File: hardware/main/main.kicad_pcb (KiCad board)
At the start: 4 copper layers, 59.7 x 109.5 mm, 220 parts, among them J101 ST_LINK, J102 USART, J301 Overvoltage_protection, J302 Rad_sensor, J303 Mos_temp, J304 Diode_temp, J601 Supplies, J801 RJ45_Shielded, J802 RJ45_Shielded, Q401 BSC093N15NS5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

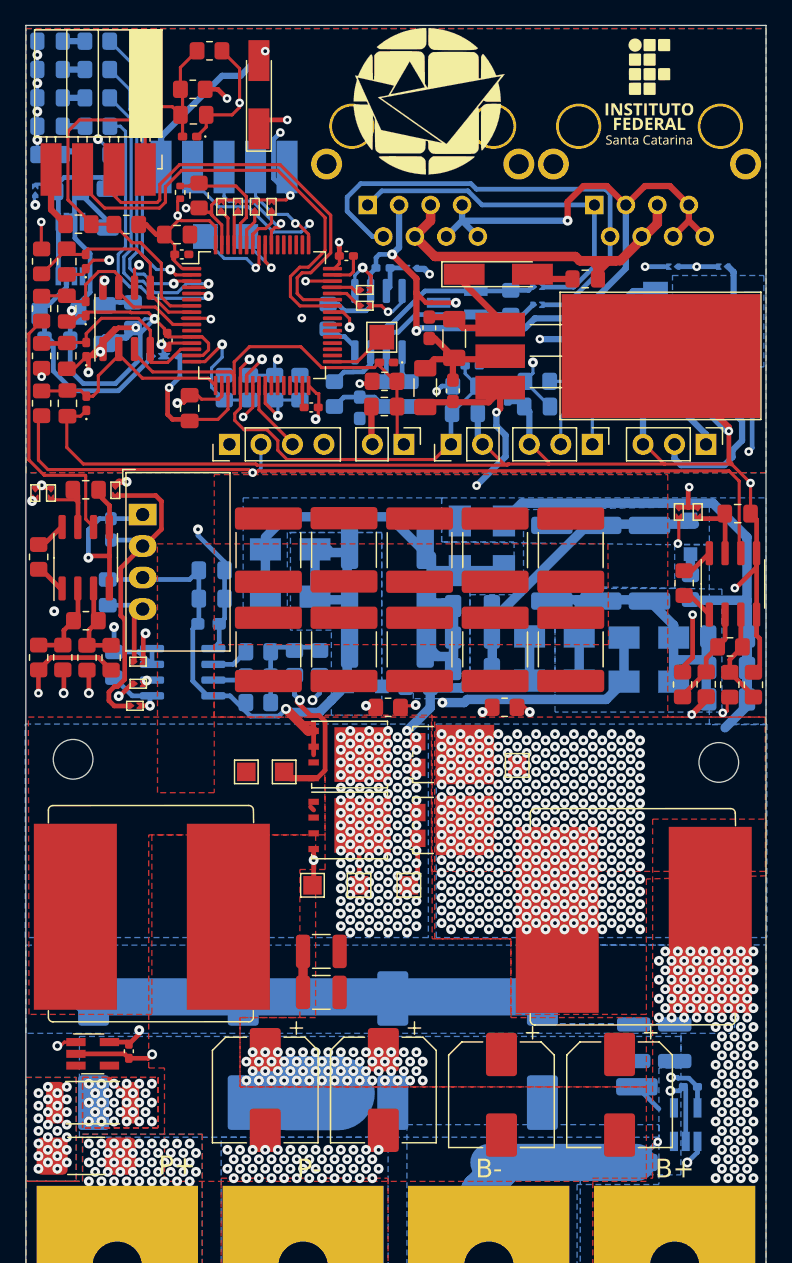
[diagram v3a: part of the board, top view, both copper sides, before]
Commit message: Layout: Silkscreen updated
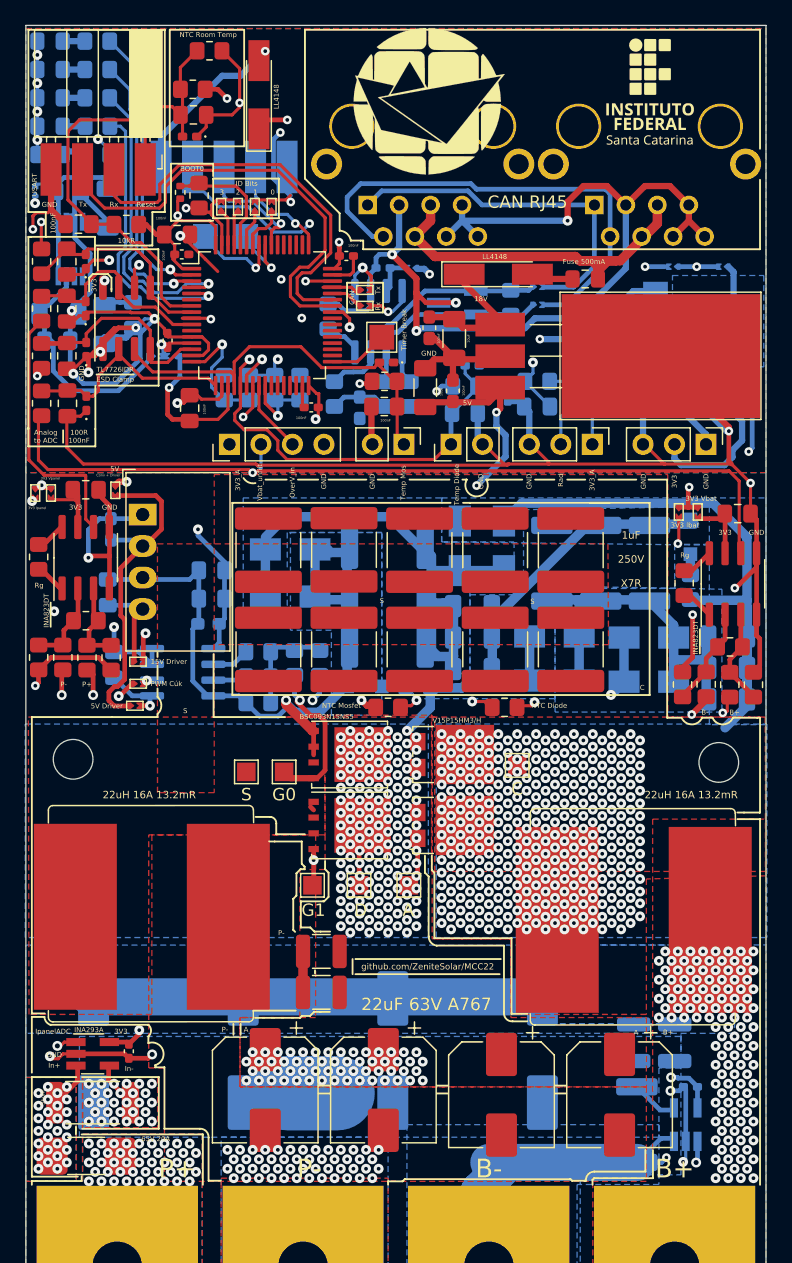
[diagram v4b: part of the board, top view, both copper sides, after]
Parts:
- added LOGO103: Logo_Open_Hardware_Small, Symbol:OSHW-Logo_5.7x6mm_SilkScreen, B.Cu at (30.8, 117.0)
- added LOGO104: Logo_Open_Hardware_Small, Zenite:symbol_logoZenite_small, B.Cu at (23.1, 117.3)
- added LOGO105: Logo_Open_Hardware_Small, Zenite:synbol_logoifsc_small, B.Cu at (37.7, 104.9)
- moved LOGO102 0.05 mm to (69.1, 87.9)
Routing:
- net GND: track 608.7 -> 973.5 mm, vias 32 -> 38
- net (no net): track 0.00 -> 4.76 mm
- net /B-: track 62.2 -> 66.8 mm
- net Net-(R321-Pad1): track 130.5 -> 133.9 mm
- net /P+: track 36.2 -> 39.0 mm
- net /Cuk/S: track 91.6 -> 90.3 mm
- net Net-(R320-Pad1): track 58.8 -> 59.7 mm
- net /Cuk/A: track 54.2 -> 54.9 mm
- net /P-: track 53.3 -> 53.9 mm
- net /Cuk/C: vias 352 -> 351
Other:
- board text added: "0"
- board text added: "1"
- board text added: "100R 100nF"
- board text added: "100V 10uF"
- board text added: "100nF"
- board text added: "10k"
- board text added: "10kR"
- board text added: "10nF"
- board text added: "10uF"
- board text added: "15V"
- board text added: "15V Driver"
- board text added: "18V"
- board text added: "1EDI60N12AF"
- board text added: "1R"
- board text added: "1uF"
- board text added: "1uF 250V X7R"
- board text added: "2"
- board text added: "22uF 100V"
- board text added: "22uF 63V A767"
- board text added: "22uH 16A 13.2mR"
- board text added: "3"
- board text added: "300R"
- board text added: "3V Ref"
- board text added: "3V3"
- board text added: "3V3 ADC"
- board text added: "3V3 Analog"
- board text added: "3V3 Ibat"
- board text added: "3V3 Ipanel"
- board text added: "3V3 MCU"
- board text added: "3V3 MCU|or| 3V Ref"
- board text added: "3V3 STM"
- board text added: "3V3 Vbat"
- board text added: "3V3 Vpanel"
- board text added: "3V3_A"
- board text added: "4.7nF"
- board text added: "4.7uF"
- board text added: "4R7"
- board text added: "4k7"
- board text added: "520R"
- board text added: "5V"
- board text added: "5V > 3V3"
- board text added: "5V CAN"
- board text added: "5V Driver"
- board text added: "5V STM"
- board text added: "65V 20A"
- board text added: "A"
- board text added: "A767"
- board text added: "AMS1117-3.3"
- board text added: "Analog to ADC"
- board text added: "BOOT0"
- board text added: "BSC093N15NS5"
- board text added: "Bat OverV"
- board text added: "C"
- board text added: "CAN"
- board text added: "CAN Busy"
- board text added: "CAN RJ45"
- board text added: "CAN_H"
- board text added: "CAN_H> <CAN_L"
- board text added: "CAN_L"
- board text added: "CAN_Rx>"
- board text added: "CAN_Tx <"
- board text added: "Conv + Driver"
- board text added: "D"
- board text added: "DB_0"
- board text added: "DB_1"
- board text added: "Diode°C"
- board text added: "Driver"
- board text added: "ESD Clamp"
- board text added: "Fuse 500mA"
- board text added: "G0"
- board text added: "G1"
- board text added: "GND"
- board text added: "ID Bits"
- board text added: "INA293A"
- board text added: "INA823DT"
- board text added: "IbatADC"
- board text added: "In+"
- board text added: "In-"
- board text added: "IpanelADC"
- board text added: "LED0"
- board text added: "LED1"
- board text added: "LL4148"
- board text added: "MCP2551"
- board text added: "Mos.°C"
- board text added: "NTC Diode"
- board text added: "NTC Mosfet"
- board text added: "NTC Room Temp"
- board text added: "Out_G"
- board text added: "OverV_in"
- board text added: "Overvoltage"
- board text added: "P+ Fused"
- board text added: "P+ Unfused"
- board text added: "PESD1CAN"
- board text added: "PWM"
- board text added: "PWM Cúk"
- board text added: "REF3430QDGKRQ1"
- board text added: "Rad"
- board text added: "Rad Sensor"
- board text added: "Reset"
- board text added: "Rg"
- board text added: "Rx"
- board text added: "S"
- board text added: "SNK"
- board text added: "SRC"
- board text added: "ST-Link"
- board text added: "SWCLK"
- board text added: "SWDIO"
- board text added: "SWO"
- board text added: "Shunt"
- board text added: "Snubber"
- board text added: "Status LED"
- board text added: "Supplies"
- board text added: "Supply ADC"
- board text added: "TL7726IDR"
- board text added: "Temp Diode"
- board text added: "Temp Mos"
- board text added: "Timer Break"
- board text added: "Tx"
- board text added: "USART"
- board text added: "V15P15HM3/H"
- board text added: "Vbat_unfilt"
- board text added: "X7R"
- board text added: "github.com/ZeniteSolar/MCC22"

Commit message: layout: Separating analogical power nets
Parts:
- removed D303, D304, D305, D306, D307, D308: ESD351DPYR, Diode_SMD:D_0402_1005Metric_Pad0.77x0.64mm_HandSolder
- added D103: ESD351DPYR, Diode_SMD:D_0402_1005Metric_Pad0.77x0.64mm_HandSolder, B.Cu at (33.8, 97.0)
- added D104: ESD351DPYR, Diode_SMD:D_0402_1005Metric_Pad0.77x0.64mm_HandSolder, B.Cu at (36.1, 97.0)
- added D105: ESD351DPYR, Diode_SMD:D_0402_1005Metric_Pad0.77x0.64mm_HandSolder, B.Cu at (38.4, 97.0)
- added D106: ESD351DPYR, Diode_SMD:D_0402_1005Metric_Pad0.77x0.64mm_HandSolder, F.Cu at (31.5, 92.2)
- added D107: ESD351DPYR, Diode_SMD:D_0402_1005Metric_Pad0.77x0.64mm_HandSolder, F.Cu at (42.9, 96.8)
- added D108: ESD351DPYR, Diode_SMD:D_0402_1005Metric_Pad0.77x0.64mm_HandSolder, F.Cu at (41.4, 96.8)
- added D413: SMF64A, Diode_SMD:D_SOD-123F, B.Cu at (73.9, 164.6)
- added D601: ESD351DPYR, Diode_SMD:D_0402_1005Metric_Pad0.77x0.64mm_HandSolder, B.Cu at (67.8, 107.4)
- added NT101: NetTie_2, Resistor_SMD:R_0201_0603Metric, F.Cu at (11.9, 100.1)
- added NT102: NetTie_2, Resistor_SMD:R_0201_0603Metric, F.Cu at (14.4, 101.8)
- added NT103: Resistor_SMD:R_0201_0603Metric, Resistor_SMD:R_0201_0603Metric, F.Cu at (14.4, 100.1)
- added NT104: NetTie_2, Resistor_SMD:R_0201_0603Metric, F.Cu at (11.9, 101.8)
- added NT201: GNDA, Resistor_SMD:R_0201_0603Metric, F.Cu at (16.3, 105.4)
- added NT202: GNDS, Resistor_SMD:R_0201_0603Metric, F.Cu at (14.7, 109.5)
- added NT203: 3V3S, Resistor_SMD:R_0201_0603Metric, F.Cu at (11.9, 105.9)
- added NT301: GNDA, Resistor_SMD:R_0201_0603Metric, F.Cu at (96.5, 107.2)
- added R408: 0R, Resistor_SMD:R_0805_2012Metric_Pad1.20x1.40mm_HandSolder, B.Cu at (72.9, 161.3)
- U601: footprint Zenite:TO-220-3_Horizontal_TabDown_SMD -> Zenite:TO-220-3_Horizontal_TabDown_SMD_3
- moved JP103 24.6 mm to (30.5, 117.3), turned to 0 degrees
- moved C202 20.6 mm to (24.9, 116.3), turned to -90 degrees
- moved C201 19.0 mm to (22.6, 116.1), turned to -90 degrees
- moved U201 14.1 mm to (27.9, 113.5), turned to 90 degrees
- moved C203 7.15 mm to (28.4, 107.2), turned to -90 degrees
- moved J302 5.05 mm to (59.4, 116.3), turned to 90 degrees
- moved J601 5.05 mm to (68.6, 116.3), turned to 90 degrees
- moved C204 4.90 mm to (26.2, 107.2), turned to -90 degrees
- moved C313 4.01 mm to (21.3, 105.4)
- moved C314 4.01 mm to (23.6, 104.7)
- moved J303 2.81 mm to (46.5, 116.1), turned to 90 degrees
- moved JP203 0.92 mm to (30.7, 108.7), turned to 90 degrees
- moved C211 0.57 mm to (30.0, 107.4)
- moved TP201 0.51 mm to (36.6, 100.1)
- moved TP202 0.51 mm to (33.3, 100.1)
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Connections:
- net /STM32/RESET renamed /RESET
- net /STM32/SWCLK renamed /SWCLK
- net /STM32/SWDIO renamed /SWDIO
- net /STM32/SWO renamed /SWO
- net /STM32/USART_RX renamed /USART_RX
- net /STM32/USART_TX renamed /USART_TX
- C203 pad 1: GND -> GNDA
- C204 pad 1: GND -> GNDA
- C211 pad 1: GND -> GNDA
- C301 pad 2: GND -> GNDA
- C302 pad 2: GND -> GNDA
- C303 pad 2: GND -> GNDA
- C304 pad 2: GND -> GNDA
- C305 pad 2: GND -> GNDA
- C306 pad 2: GND -> GNDA
- C307 pad 2: GND -> GNDA
- C308 pad 2: GND -> GNDA
- C309 pad 2: GND -> GNDA
- C310 pad 2: GND -> GNDA
- C311 pad 2: GND -> GNDA
- C312 pad 2: GND -> GNDA
- C313 pad 2: GND -> GNDA
- C314 pad 2: GND -> GNDA
- C315 pad 2: GND -> GNDA
- D301 pad 1: GND -> GNDA
- D302 pad 1: GND -> GNDA
- J301 pad 4: GND -> GNDA
- J302 pad 3: GND -> GNDA
- J303 pad 2: GND -> GNDA
- J304 pad 2: GND -> GNDA
- R304 pad 2: GND -> GNDA
- R310 pad 1: GND -> GNDA
- R312 pad 2: GND -> GNDA
- R313 pad 1: GND -> GNDA
- R315 pad 2: GND -> GNDA
- R323 pad 1: GND -> GNDA
- R325 pad 1: GND -> GNDA
- TH301 pad 2: GND -> GNDA
- TH302 pad 2: GND -> GNDA
- TH303 pad 2: GND -> GNDA
- U201 pad 2: GND -> Net-(U201-Pad2)
- U201 pad 6: /STM32/3V_Ref -> Net-(U201-Pad6)
- U202 pad 12: GND -> GNDA
- U202 pad 15: GND -> GNDA
- U301 pad 4: GND -> GNDA
- U301 pad 5: GND -> GNDA
- U302 pad 4: GND -> GNDA
- U302 pad 5: GND -> GNDA
- U303 pad 2: GND -> GNDA
- U304 pad 2: GND -> GNDA
- U305 pad 1: GND -> GNDA
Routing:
- net GND: track 973.5 -> 819.7 mm, vias 38 -> 31
- net GNDA: track 0.00 -> 145.1 mm, vias 0 -> 4
- net +5V: track 124.1 -> 94.6 mm, vias 6 -> 5
- net Net-(U201-Pad2): track 0.00 -> 13.6 mm
- net /STM32/3V_Ref: track 19.7 -> 7.59 mm
- net /USART_TX: track 35.5 -> 39.4 mm
- net /USART_RX: track 34.4 -> 38.0 mm
- net /3V3_Analog: track 160.3 -> 156.9 mm, vias 8 -> 9
- net /RESET: track 29.7 -> 33.0 mm
- net /Analog/V_temp_mos: track 52.8 -> 56.1 mm
- net Net-(U201-Pad6): track 0.00 -> 2.64 mm
- net /STM32/3V3_MCU: track 106.3 -> 108.8 mm, vias 5 -> 6
- net /Cuk/A: track 54.9 -> 57.3 mm
- net +3V3: track 31.1 -> 33.1 mm
- net Net-(D413-Pad1): track 0.00 -> 1.91 mm
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
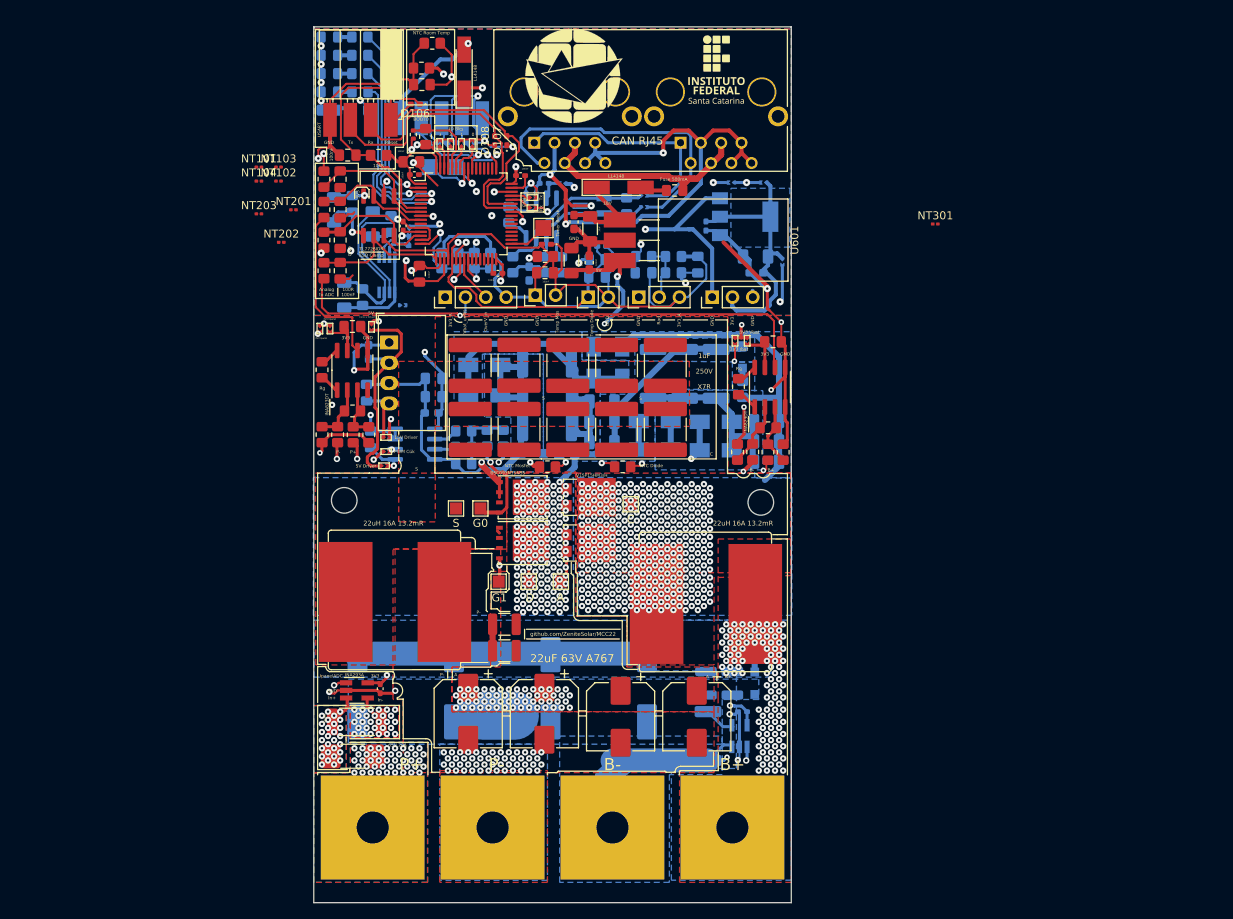
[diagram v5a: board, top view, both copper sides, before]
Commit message: Layout: Place components and route analog, supplies and CAN
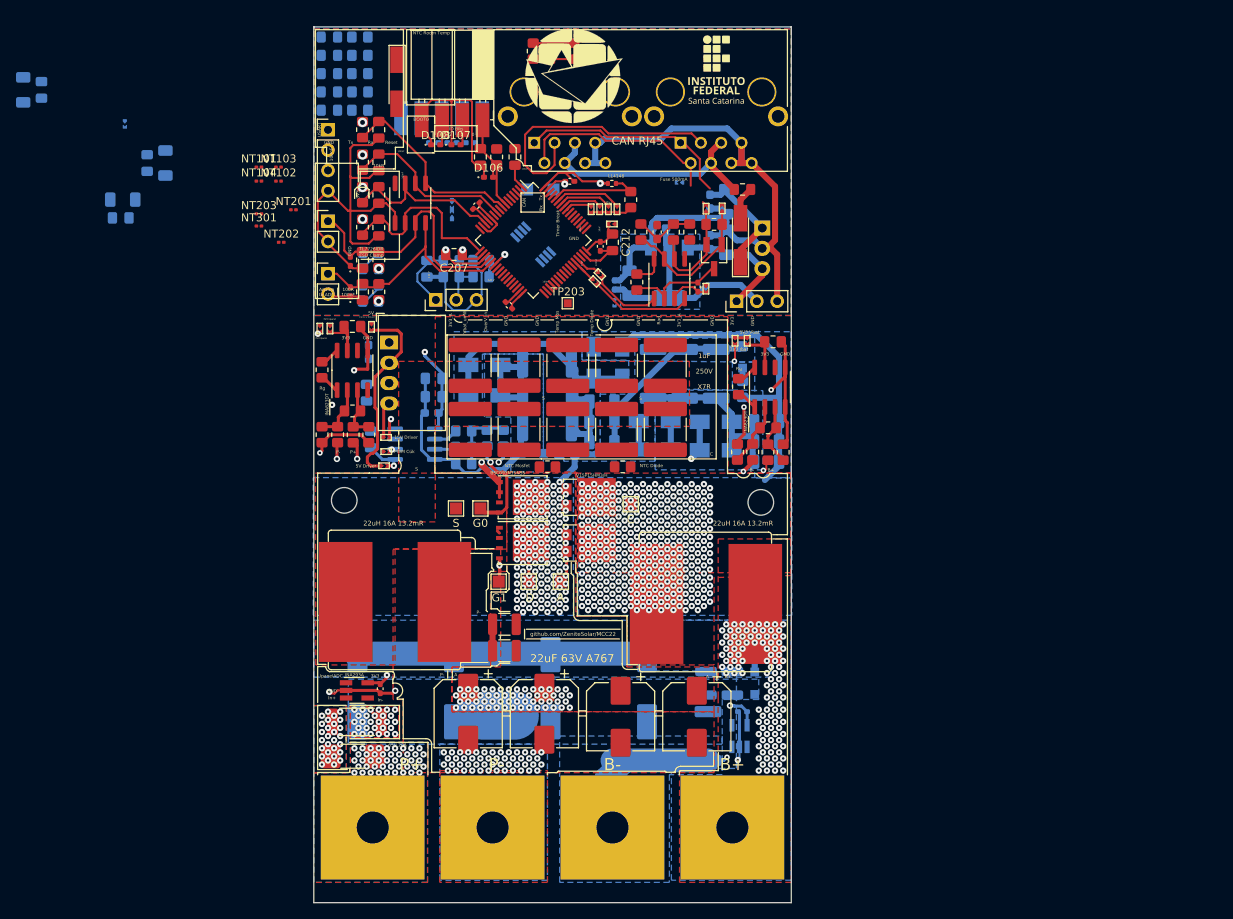
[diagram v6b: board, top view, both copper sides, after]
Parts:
- added C212: 25V 10uF X5R ±10% 0805, Capacitor_SMD:C_0805_2012Metric_Pad1.18x1.45mm_HandSolder, F.Cu at (56.1, 109.5)
- C302, C701, C702, D301, D701, JP105, JP109, JP110, JP201, R302, R701, R702, R703, R704, R705, U701: moved to F.Cu
- C601, C602, C603, C604: moved to B.Cu
- TP201, TP202: footprint TestPoint:TestPoint_Pad_2.0x2.0mm -> TestPoint:TestPoint_Pad_1.5x1.5mm
- TP203: footprint TestPoint:TestPoint_Pad_2.0x2.0mm -> TestPoint:TestPoint_Pad_1.0x1.0mm
- U601: footprint Zenite:TO-220-3_Horizontal_TabDown_SMD_3 -> Package_TO_SOT_THT:TO-220-3_Vertical; moved to B.Cu
- moved NT301 84.6 mm to (11.9, 107.4)
- moved C313 41.7 mm to (-17.5, 90.4)
- moved JP103 41.7 mm to (-4.82, 95.3), turned to -90 degrees
- moved C314 41.4 mm to (-15.2, 90.4)
- moved C301 33.9 mm to (32.9, 112.8), turned to -90 degrees
- moved J304 32.6 mm to (20.6, 113.4), turned to 0 degrees
- moved D301 31.9 mm to (23.4, 115.7), turned to 90 degrees
- moved C202 31.8 mm to (-5.33, 106.4), turned to 0 degrees
- moved C203 31.4 mm to (-2.03, 99.6), turned to 90 degrees
- moved C201 30.2 mm to (-5.08, 104.1), turned to 0 degrees
- moved C302 29.4 mm to (24.9, 115.7), turned to -90 degrees
- moved R304 27.9 mm to (36.0, 113.8), turned to 180 degrees
- moved R303 27.8 mm to (36.0, 111.8), turned to 0 degrees
- moved R302 27.6 mm to (26.9, 115.7), turned to -90 degrees
- moved J303 27.5 mm to (20.6, 106.8), turned to 0 degrees
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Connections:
- C201 pad 1: GND -> GNDA
- C202 pad 1: GND -> GNDA
- C501 pad 1: GND -> /Cuk/S
- C501 pad 2: /5V_Driver -> Net-(JP501-Pad1)
- C502 pad 1: Net-(C502-Pad1) -> /5V_Driver
- C502 pad 2: /Cuk/S -> GND
- JP204 pad 1: Net-(JP204-Pad1) -> Net-(U202-Pad56)
- JP205 pad 1: Net-(JP205-Pad1) -> Net-(U202-Pad57)
- JP206 pad 1: Net-(JP206-Pad1) -> Net-(U202-Pad58)
- JP207 pad 1: Net-(JP207-Pad1) -> Net-(U202-Pad59)
- JP501 pad 1: Net-(C502-Pad1) -> Net-(JP501-Pad1)
- PS501 pad 4: Net-(C502-Pad1) -> Net-(JP501-Pad1)
- TP201 pad 1: Net-(TP201-Pad1) -> Net-(U202-Pad61)
- TP202 pad 1: Net-(TP202-Pad1) -> Net-(U202-Pad62)
- U201 pad 3: GND -> GNDA
- U202 pad 56: Net-(TP201-Pad1) -> Net-(U202-Pad56)
- U202 pad 57: Net-(TP202-Pad1) -> Net-(U202-Pad57)
- U202 pad 58: Net-(JP204-Pad1) -> Net-(U202-Pad58)
- U202 pad 59: Net-(JP205-Pad1) -> Net-(U202-Pad59)
- U202 pad 61: Net-(JP206-Pad1) -> Net-(U202-Pad61)
- U202 pad 62: Net-(JP207-Pad1) -> Net-(U202-Pad62)
- U305 pad 4: /Analog/I_panel_adc+ -> /Analog/V_temp_diode
- U305 pad 6: /Analog/V_temp_diode -> /Analog/V_panel_adc+
- U305 pad 7: /Analog/V_panel_adc+ -> /Analog/I_panel_adc+
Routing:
- net GND: track 819.7 -> 180.9 mm, vias 31 -> 2
- net GNDA: track 145.1 -> 368.2 mm, vias 4 -> 8
- net /3V3_Analog: track 156.9 -> 21.2 mm, vias 9 -> 2
- net Net-(R321-Pad1): track 134.2 -> 0.00 mm, vias 2 -> 1
- net /STM32/3V3_MCU: track 108.8 -> 28.8 mm, vias 6 -> 2
- net +5V: track 94.6 -> 15.8 mm, vias 5 -> 0
- net Net-(R320-Pad1): track 59.7 -> 0.00 mm, vias 2 -> 1
- net /Analog/V_bat_unfiltered+: track 69.6 -> 10.4 mm
- net /PWM: track 52.1 -> 0.00 mm, vias 2 -> 0
- net /Analog/V_temp_diode: track 73.1 -> 28.0 mm, vias 3 -> 0
- net /3V3_STM: track 44.5 -> 0.00 mm, vias 2 -> 0
- net /STM32/Bat_OverV_Out: track 36.8 -> 0.00 mm, vias 2 -> 0
- net /USART_TX: track 39.4 -> 3.16 mm
- net /USART_RX: track 38.0 -> 3.16 mm
- net /Analog/V_Rad: track 34.6 -> 7.49 mm, vias 2 -> 1
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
